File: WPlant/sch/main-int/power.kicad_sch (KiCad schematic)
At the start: 32 parts, among them J5 220V, U3 AP64352SP-13, U4 AP64352SP-13, U6 AP2204R-5.0

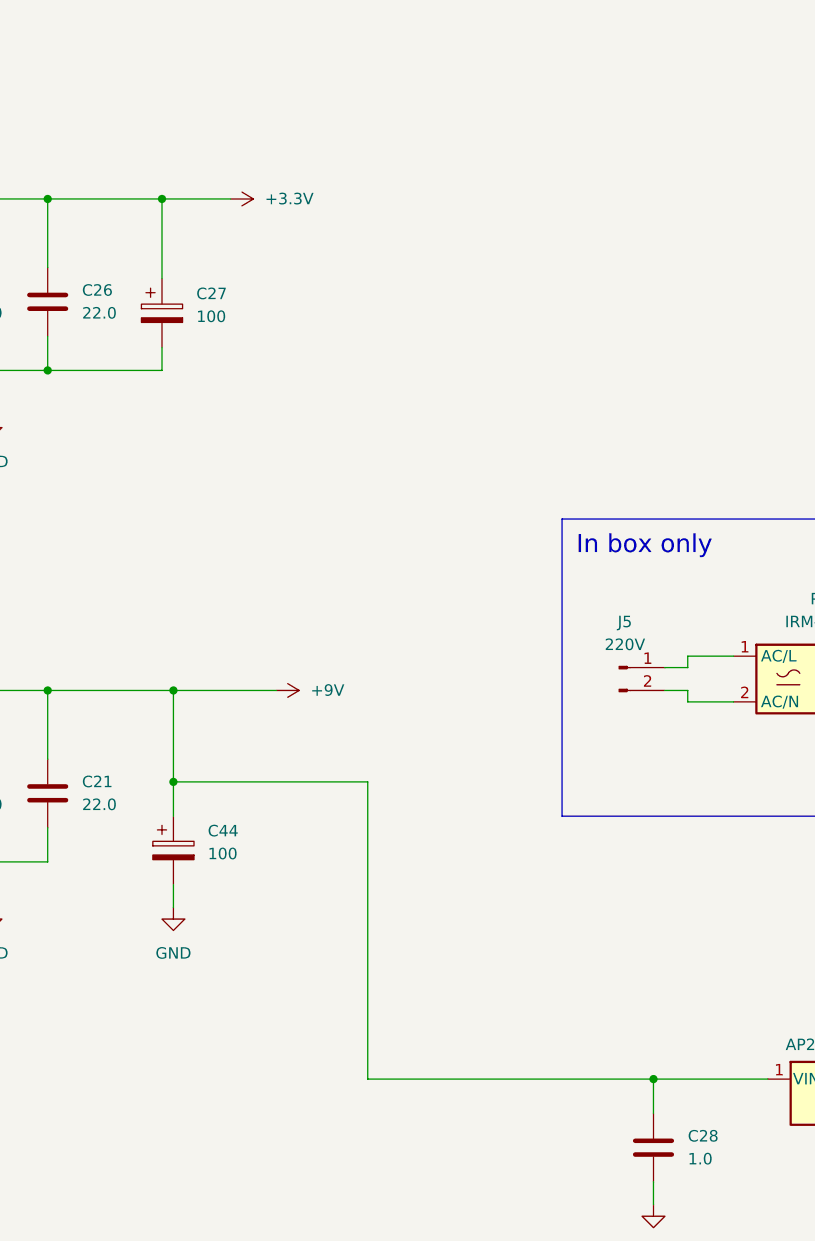
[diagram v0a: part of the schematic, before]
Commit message: Added jumpers to power lines for Main-* schematics
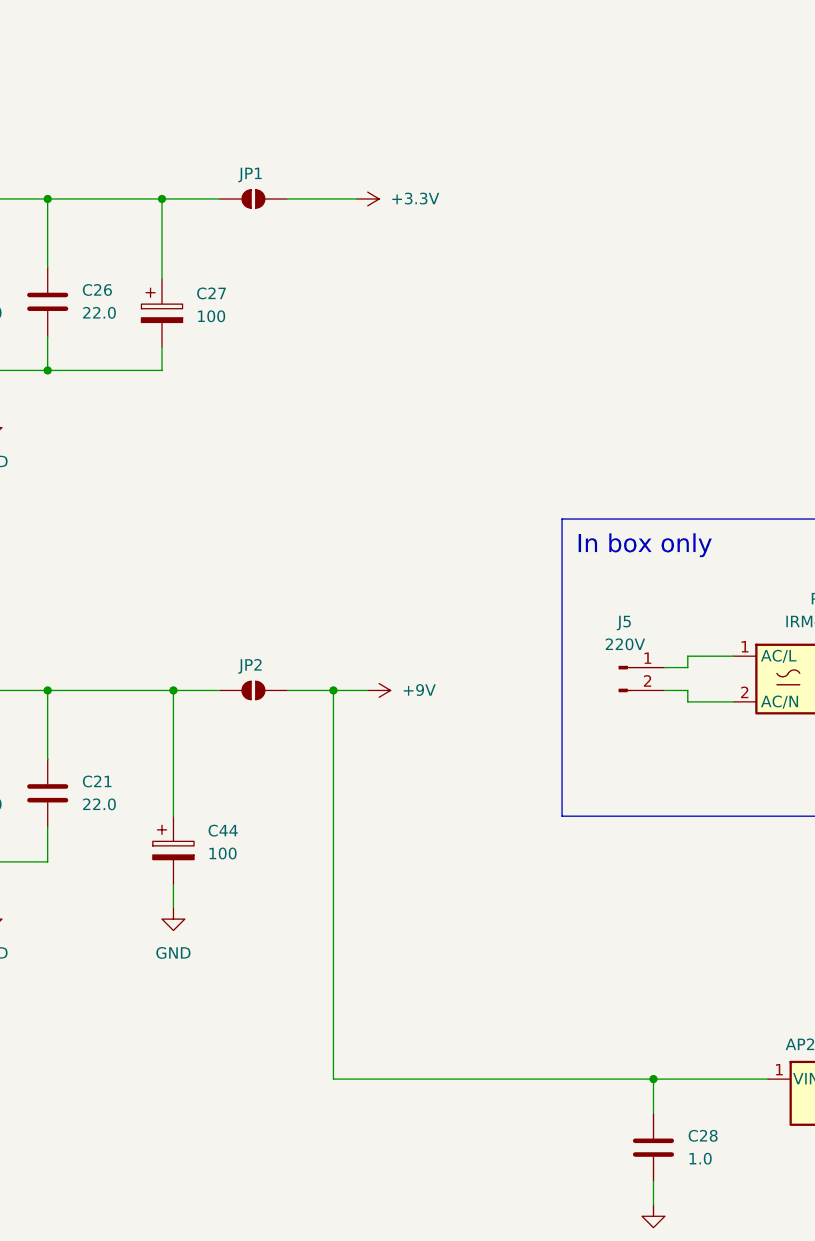
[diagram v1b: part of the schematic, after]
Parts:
- added JP1, JP2: SolderJumper_2_Open, Jumper:SolderJumper-2_P1.3mm_Open_RoundedPad1.0x1.5mm, symbol Jumper:SolderJumper_2_Open
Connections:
- net +3.3V: now also JP1.2 (B); no longer C16.2, C25.2, C26.2, C27.1, L3.2, R17.1
- net +9V: now also JP2.2 (B); no longer C19.2, C20.2, C21.2, C44.1, L2.2, R14.1
- new net: C16.2, C25.2, C26.2, C27.1, JP1.1 (A), L3.2, R17.1
- new net: C19.2, C20.2, C21.2, C44.1, JP2.1 (A), L2.2, R14.1
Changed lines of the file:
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@@
 	)
 	(junction
+		(at 173.99 96.52)
+		(diameter 0)
+		(color 0 0 0 0)
+	)
+	(junction
 		(at 107.95 109.22)
 		(diameter 0)
@@
 	)
 	(junction
-		(at 156.21 106.68)
-		(diameter 0)
-		(color 0 0 0 0)
-	)
-	(junction
 		(at 135.89 115.57)
 		(diameter 0)
@@
 	(wire
 		(pts
-			(xy 156.21 96.52) (xy 156.21 106.68)
+			(xy 156.21 96.52) (xy 156.21 110.49)
 		)
 		(stroke
@@
 	(wire
 		(pts
+			(xy 168.91 96.52) (xy 173.99 96.52)
+		)
+		(stroke
+			(width 0)
+			(type default)
+		)
+	)
+	(wire
+		(pts
 			(xy 107.95 54.61) (xy 107.95 55.88)
 		)
@@
 	(wire
 		(pts
-			(xy 177.8 139.7) (xy 177.8 106.68)
+			(xy 173.99 96.52) (xy 173.99 139.7)
 		)
 		(stroke
@@
 	(wire
 		(pts
+			(xy 173.99 96.52) (xy 177.8 96.52)
+		)
+		(stroke
+			(width 0)
+			(type default)
+		)
+	)
+	(wire
+		(pts
 			(xy 81.28 104.14) (xy 99.06 104.14)
 		)
@@
 	(wire
 		(pts
-			(xy 156.21 106.68) (xy 156.21 110.49)
-		)
-		(stroke
-			(width 0)
-			(type default)
-		)
-	)
-	(wire
-		(pts
 			(xy 107.95 109.22) (xy 107.95 110.49)
 		)
@@
 	(wire
 		(pts
+			(xy 168.91 41.91) (xy 176.53 41.91)
+		)
+		(stroke
+			(width 0)
+			(type default)
+		)
+	)
+	(wire
+		(pts
 			(xy 129.54 111.76) (xy 129.54 115.57)
 		)
@@
 	(wire
 		(pts
-			(xy 177.8 139.7) (xy 209.55 139.7)
+			(xy 173.99 139.7) (xy 209.55 139.7)
 		)
 		(stroke
@@
 	(wire
 		(pts
-			(xy 154.94 41.91) (xy 162.56 41.91)
+			(xy 154.94 41.91) (xy 161.29 41.91)
 		)
 		(stroke
@@
 	(wire
 		(pts
-			(xy 156.21 96.52) (xy 167.64 96.52)
+			(xy 156.21 96.52) (xy 161.29 96.52)
 		)
 		(stroke
@@
 	(wire
 		(pts
-			(xy 156.21 106.68) (xy 177.8 106.68)
-		)
-		(stroke
-			(width 0)
-			(type default)
-		)
-	)
-	(wire
-		(pts
 			(xy 129.54 60.96) (xy 135.89 60.96)
 		)
@@
 	(symbol
 		(lib_id "power:+3.3V")
-		(at 162.56 41.91 270)
+		(at 176.53 41.91 270)
 		(unit 1)
 		(exclude_from_sim no)
@@
 		(fields_autoplaced yes)
 		(property "Reference" "#PWR040"
-			(at 158.75 41.91 0)
+			(at 172.72 41.91 0)
 			(effects
 				(font
@@
 		)
 		(property "Value" "+3.3V"
-			(at 166.37 41.9099 90)
+			(at 180.34 41.9099 90)
 			(effects
 				(font
@@
 		)
 		(property "Footprint" ""
-			(at 162.56 41.91 0)
+			(at 176.53 41.91 0)
 			(effects
 				(font
@@
 		)
 		(property "Datasheet" ""
-			(at 162.56 41.91 0)
+			(at 176.53 41.91 0)
 			(effects
 				(font
@@
 		)
 		(property "Description" "Power symbol creates a global label with name \"+3.3V\""
-			(at 162.56 41.91 0)
+			(at 176.53 41.91 0)
 			(effects
 				(font
@@
 	)
 	(symbol
+		(lib_id "Jumper:SolderJumper_2_Open")
+		(at 165.1 41.91 0)
+		(unit 1)
+		(exclude_from_sim yes)
+		(in_bom no)
+		(on_board yes)
+		(dnp no)
+		(property "Reference" "JP1"
+			(at 164.846 39.116 0)
+			(effects
+				(font
+					(size 1.27 1.27)
+				)
+			)
+		)
+		(property "Value" "SolderJumper_2_Open"
+			(at 165.1 38.1 0)
+			(effects
+				(font
+					(size 1.27 1.27)
+				)
+				(hide yes)
+			)
+		)
+		(property "Footprint" "Jumper:SolderJumper-2_P1.3mm_Open_RoundedPad1.0x1.5mm"
+			(at 165.1 41.91 0)
+			(effects
+				(font
+					(size 1.27 1.27)
+				)
+				(hide yes)
+			)
+		)
+		(property "Datasheet" "~"
+			(at 165.1 41.91 0)
+			(effects
+				(font
+					(size 1.27 1.27)
+				)
+				(hide yes)
+			)
+		)
+		(property "Description" "Solder Jumper, 2-pole, open"
+			(at 165.1 41.91 0)
+			(effects
+				(font
+					(size 1.27 1.27)
+				)
+				(hide yes)
+			)
+		)
+		(pin "1"
+		)
+		(pin "2"
+		)
+		(instances
+			(project ""
+				(path "/71bd3f7f-463d-4a2c-bec7-ca56c2fe6cec/e5010fd4-921a-4703-b472-3554db39dd22"
+					(reference "JP1")
+					(unit 1)
+				)
+			)
+		)
+	)
+	(symbol
 		(lib_id "Device:C")
 		(at 38.1 106.68 180)
@@
 	)
 	(symbol
+		(lib_id "Jumper:SolderJumper_2_Open")
+		(at 165.1 96.52 0)
+		(unit 1)
+		(exclude_from_sim yes)
+		(in_bom no)
+		(on_board yes)
+		(dnp no)
+		(property "Reference" "JP2"
+			(at 164.846 93.726 0)
+			(effects
+				(font
+					(size 1.27 1.27)
+				)
+			)
+		)
+		(property "Value" "SolderJumper_2_Open"
+			(at 165.1 92.71 0)
+			(effects
+				(font
+					(size 1.27 1.27)
+				)
+				(hide yes)
+			)
+		)
+		(property "Footprint" "Jumper:SolderJumper-2_P1.3mm_Open_RoundedPad1.0x1.5mm"
+			(at 165.1 96.52 0)
+			(effects
+				(font
+					(size 1.27 1.27)
+				)
+				(hide yes)
+			)
+		)
+		(property "Datasheet" "~"
+			(at 165.1 96.52 0)
+			(effects
+				(font
+					(size 1.27 1.27)
+				)
+				(hide yes)
+			)
+		)
+		(property "Description" "Solder Jumper, 2-pole, open"
+			(at 165.1 96.52 0)
+			(effects
+				(font
+					(size 1.27 1.27)
+				)
+				(hide yes)
+			)
+		)
+		(pin "1"
+		)
+		(pin "2"
+		)
+		(instances
+			(project "main-int"
+				(path "/71bd3f7f-463d-4a2c-bec7-ca56c2fe6cec/e5010fd4-921a-4703-b472-3554db39dd22"
+					(reference "JP2")
+					(unit 1)
+				)
+			)
+		)
+	)
+	(symbol
 		(lib_id "Device:C")
 		(at 118.11 48.26 180)
@@
 	(symbol
 		(lib_id "power:+9V")
-		(at 167.64 96.52 270)
+		(at 177.8 96.52 270)
 		(unit 1)
 		(exclude_from_sim no)
@@
 		(fields_autoplaced yes)
 		(property "Reference" "#PWR063"
-			(at 163.83 96.52 0)
+			(at 173.99 96.52 0)
 			(effects
 				(font
@@
 		)
 		(property "Value" "+9V"
-			(at 171.45 96.5199 90)
+			(at 181.61 96.5199 90)
 			(effects
 				(font
@@
 		)
 		(property "Footprint" ""
-			(at 167.64 96.52 0)
+			(at 177.8 96.52 0)
 			(effects
 				(font
@@
 		)
 		(property "Datasheet" ""
-			(at 167.64 96.52 0)
+			(at 177.8 96.52 0)
 			(effects
 				(font
@@
 		)
 		(property "Description" "Power symbol creates a global label with name \"+9V\""
-			(at 167.64 96.52 0)
+			(at 177.8 96.52 0)
 			(effects
 				(font

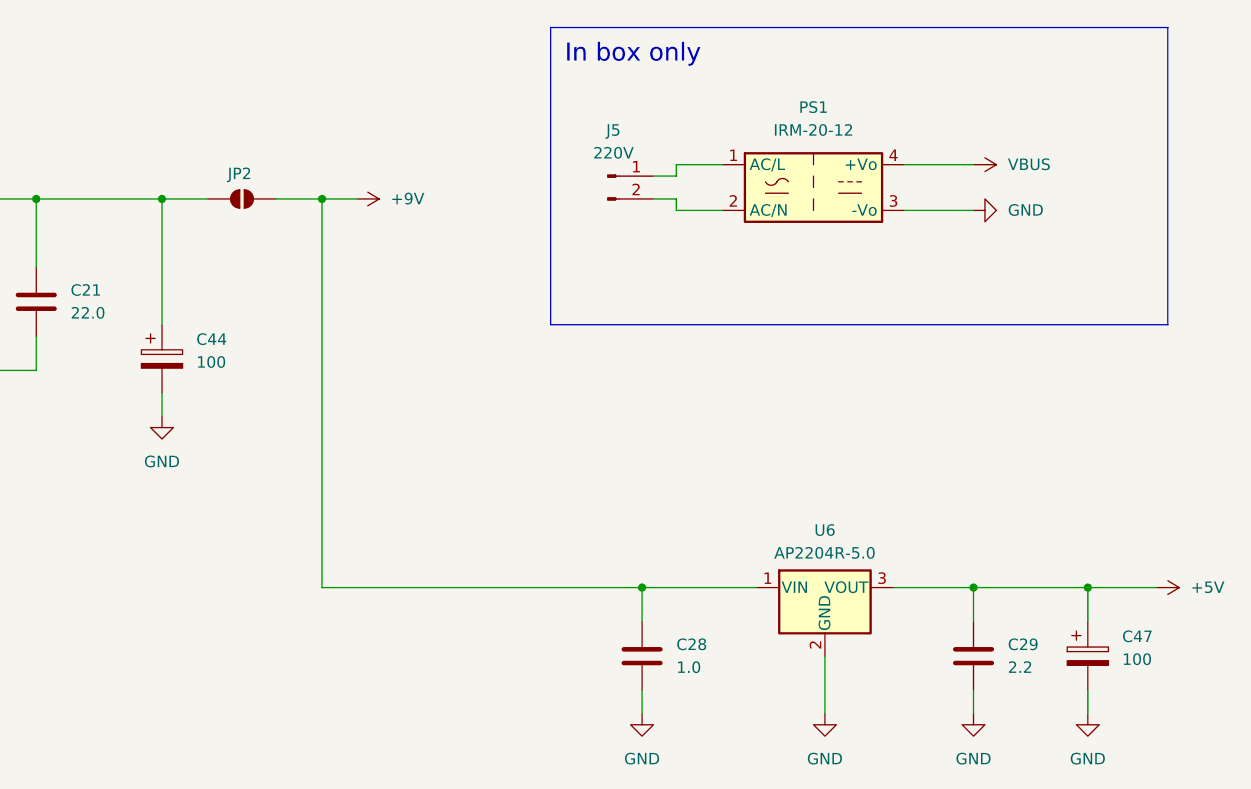
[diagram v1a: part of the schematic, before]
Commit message: Added more jumpers to power lines for Main-* schematics
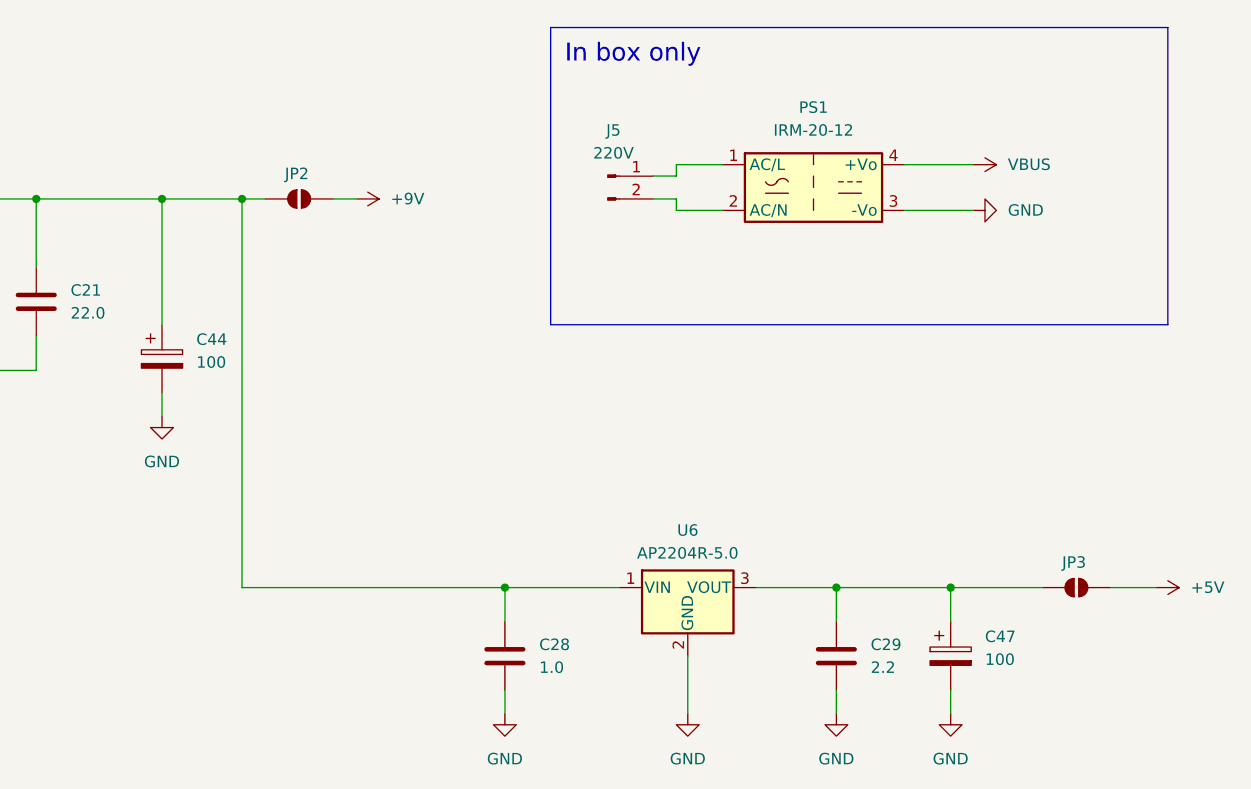
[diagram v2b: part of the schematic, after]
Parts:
- added JP3: SolderJumper_2_Open, Jumper:SolderJumper-2_P1.3mm_Open_RoundedPad1.0x1.5mm, symbol Jumper:SolderJumper_2_Open
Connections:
- net +5V: now also JP3.2 (B); no longer C29.2, C47.1, U6.3 (VOUT)
- net +9V: no longer C28.2, U6.1 (VIN)
- net at C19.2, C20.2, C21.2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: now also C28.2, U6.1 (VIN)
- new net: C29.2, C47.1, JP3.1 (A), U6.3 (VOUT)
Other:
- moved on the sheet: C28, C29, C47, JP2, U6

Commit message: Addeed places for latches on Extension board. Updated MainInt sch and pcb
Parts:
- U3, U4: footprint easyeda2kicad:SO-8_L4.9-W3.9-P1.27-LS6.0-BL-EP -> locals:SO-8_L4.9-W3.9-P1.27-LS6.0-BL-EP
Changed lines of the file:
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@@
 			)
 		)
-		(property "Footprint" "easyeda2kicad:SO-8_L4.9-W3.9-P1.27-LS6.0-BL-EP"
+		(property "Footprint" "locals:SO-8_L4.9-W3.9-P1.27-LS6.0-BL-EP"
 			(at 69.85 111.76 0)
 			(effects
@@
 			)
 		)
-		(property "Footprint" "easyeda2kicad:SO-8_L4.9-W3.9-P1.27-LS6.0-BL-EP"
+		(property "Footprint" "locals:SO-8_L4.9-W3.9-P1.27-LS6.0-BL-EP"
 			(at 69.85 57.15 0)
 			(effects

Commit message: Started routing of MainInt
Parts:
- C16, C20, C21, C26: footprint Capacitor_SMD:C_1206_3216Metric_Pad1.33x1.80mm_HandSolder -> Capacitor_SMD:C_1210_3225Metric_Pad1.33x2.70mm_HandSolder
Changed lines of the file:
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@@
 			)
 		)
-		(property "Footprint" "Capacitor_SMD:C_1206_3216Metric_Pad1.33x1.80mm_HandSolder"
+		(property "Footprint" "Capacitor_SMD:C_1210_3225Metric_Pad1.33x2.70mm_HandSolder"
 			(at 141.2748 104.14 0)
 			(effects
@@
 			)
 		)
-		(property "Footprint" "Capacitor_SMD:C_1206_3216Metric_Pad1.33x1.80mm_HandSolder"
+		(property "Footprint" "Capacitor_SMD:C_1210_3225Metric_Pad1.33x2.70mm_HandSolder"
 			(at 141.2748 49.53 0)
 			(effects
@@
 			)
 		)
-		(property "Footprint" "Capacitor_SMD:C_1206_3216Metric_Pad1.33x1.80mm_HandSolder"
+		(property "Footprint" "Capacitor_SMD:C_1210_3225Metric_Pad1.33x2.70mm_HandSolder"
 			(at 128.5748 104.14 0)
 			(effects
@@
 			)
 		)
-		(property "Footprint" "Capacitor_SMD:C_1206_3216Metric_Pad1.33x1.80mm_HandSolder"
+		(property "Footprint" "Capacitor_SMD:C_1210_3225Metric_Pad1.33x2.70mm_HandSolder"
 			(at 128.5748 49.53 0)
 			(effects

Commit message: Update WP Sch (sheets titles, replaced wires by bus, update components values)
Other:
- title: Power module -> Power module (WPMain Internal)
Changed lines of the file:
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@@
 	(paper "A4")
 	(title_block
-		(title "Power module")
+		(title "Power module (WPMain Internal)")
+		(date "2026-02-05")
 		(company "RoboWay")
 	)
